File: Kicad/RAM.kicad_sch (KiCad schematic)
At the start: 14 parts, among them U6 74LVC245, U7 74LVC245, U8 MT48LC4M16A2P

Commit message: PCB: Start routing PCB
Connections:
- net D0: now also U7.18 (B0); no longer U6.18 (B0)
- net D1: now also U7.17 (B1); no longer U6.17 (B1)
- net D10: now also U6.16 (B2); no longer U7.16 (B2)
- net D11: now also U6.15 (B3); no longer U7.15 (B3)
- net D12: now also U6.14 (B4); no longer U7.14 (B4)
- net D13: now also U6.13 (B5); no longer U7.13 (B5)
- net D14: now also U6.12 (B6); no longer U7.12 (B6)
- net D15: now also U6.11 (B7); no longer U7.11 (B7)
- net D2: now also U7.16 (B2); no longer U6.16 (B2)
- net D3: now also U7.15 (B3); no longer U6.15 (B3)
- net D4: now also U7.14 (B4); no longer U6.14 (B4)
- net D5: now also U7.11 (B7); no longer U6.11 (B7)
- net D6: now also U7.12 (B6); no longer U6.12 (B6)
- net D7: now also U7.13 (B5); no longer U6.13 (B5)
- net D8: now also U6.18 (B0); no longer U7.18 (B0)
- net D9: now also U6.17 (B1); no longer U7.17 (B1)
- net R_D0: now also U7.2 (A0), U8.2 (DQ0); no longer U6.2 (A0), U8.13 (DQ7)
- net R_D1: now also U7.3 (A1), U8.4 (DQ1); no longer U6.3 (A1), U8.11 (DQ6)
- net R_D10: now also U6.4 (A2), U8.45 (DQ10); no longer U7.4 (A2), U8.50 (DQ13)
- net R_D11: now also U6.5 (A3), U8.47 (DQ11); no longer U7.5 (A3), U8.48 (DQ12)
- net R_D12: now also U6.6 (A4), U8.48 (DQ12); no longer U7.6 (A4), U8.47 (DQ11)
- net R_D13: now also U6.7 (A5), U8.50 (DQ13); no longer U7.7 (A5), U8.45 (DQ10)
- net R_D14: now also U6.8 (A6), U8.51 (DQ14); no longer U7.8 (A6), U8.44 (DQ9)
- net R_D15: now also U6.9 (A7), U8.53 (DQ15); no longer U7.9 (A7), U8.42 (DQ8)
- net R_D2: now also U7.4 (A2), U8.5 (DQ2); no longer U6.4 (A2), U8.10 (DQ5)
- net R_D3: now also U7.5 (A3), U8.7 (DQ3); no longer U6.5 (A3), U8.8 (DQ4)
- net R_D4: now also U7.6 (A4), U8.8 (DQ4); no longer U6.6 (A4), U8.7 (DQ3)
- net R_D5: now also U7.7 (A5), U8.10 (DQ5); no longer U6.7 (A5), U8.5 (DQ2)
- net R_D6: now also U7.8 (A6), U8.11 (DQ6); no longer U6.8 (A6), U8.4 (DQ1)
- net R_D7: now also U7.9 (A7), U8.13 (DQ7); no longer U6.9 (A7), U8.2 (DQ0)
- net R_D8: now also U6.2 (A0), U8.42 (DQ8); no longer U7.2 (A0), U8.53 (DQ15)
- net R_D9: now also U6.3 (A1), U8.44 (DQ9); no longer U7.3 (A1), U8.51 (DQ14)
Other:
- moved on the sheet: C15, C16, C17, C18, C19, C20, C21, C22, C23, C24, C25, U6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

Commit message: PCB: More routing...
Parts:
- U8: value MT48LC4M16A2P -> MT48LC8M16A2P
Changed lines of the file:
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@@
     (in_bom yes) (on_board yes) (fields_autoplaced)
     (property "Reference" "U8" (id 0) (at 182.245 98.425 0))
-    (property "Value" "MT48LC4M16A2P" (id 1) (at 182.245 100.965 0))
+    (property "Value" "MT48LC8M16A2P" (id 1) (at 182.245 100.965 0))
     (property "Footprint" "Package_SO:TSOP-II-54_22.2x10.16mm_P0.8mm" (id 2) (at 153.67 92.71 0)
       (effects (font (size 1.27 1.27)) hide)
     )
-    (property "Datasheet" "" (id 3) (at 153.67 92.71 0)
+    (property "Datasheet" "https://media.digikey.com/pdf/Data%20Sheets/Micron%20Technology%20Inc%20PDFs/MT48LC%208M16A2,16M8A2,32M4A2.pdf" (id 3) (at 153.67 92.71 0)
       (effects (font (size 1.27 1.27)) hide)
     )
@@
     (in_bom yes) (on_board yes) (fields_autoplaced)
     (property "Reference" "U8" (id 0) (at 182.88 29.21 0))
-    (property "Value" "MT48LC4M16A2P" (id 1) (at 182.88 31.75 0))
+    (property "Value" "MT48LC8M16A2P" (id 1) (at 182.88 31.75 0))
     (property "Footprint" "Package_SO:TSOP-II-54_22.2x10.16mm_P0.8mm" (id 2) (at 154.305 43.815 0)
       (effects (font (size 1.27 1.27)) hide)
     )
-    (property "Datasheet" "" (id 3) (at 154.305 43.815 0)
+    (property "Datasheet" "https://media.digikey.com/pdf/Data%20Sheets/Micron%20Technology%20Inc%20PDFs/MT48LC%208M16A2,16M8A2,32M4A2.pdf" (id 3) (at 154.305 43.815 0)
       (effects (font (size 1.27 1.27)) hide)
     )

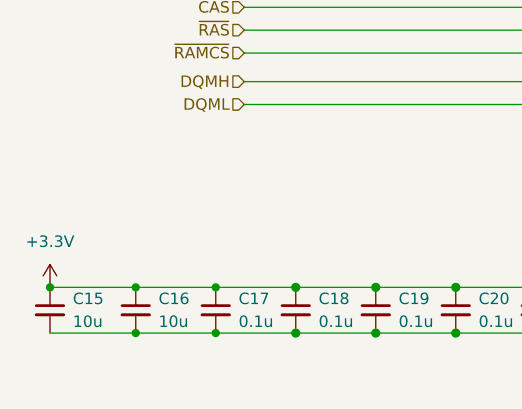
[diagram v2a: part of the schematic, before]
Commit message: PCB: More work...
* Add DIP Switches for Ram/Rom/IDE config
* Route bank select signals for Flash rom
* Flip IDE to bottom of the board
* Add some bulk capacitors
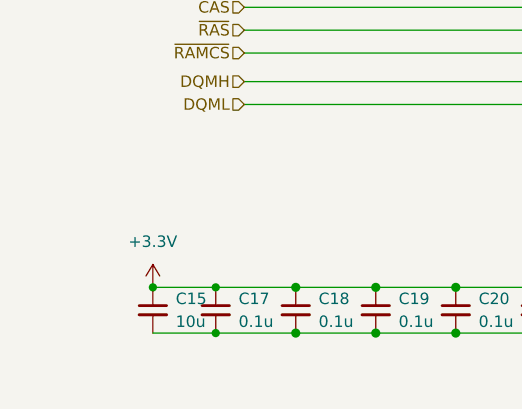
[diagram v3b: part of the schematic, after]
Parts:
- removed C16: 10u, Capacitor_SMD:C_0805_2012Metric_Pad1.18x1.45mm_HandSolder, symbol Device:C_Small
- C15: footprint Capacitor_SMD:C_0805_2012Metric_Pad1.18x1.45mm_HandSolder -> Capacitor_Tantalum_SMD:CP_EIA-3216-18_Kemet-A; LCSC # C15850 -> C117023
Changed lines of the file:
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@@
   (junction (at 170.815 116.205) (diameter 1.016) (color 0 0 0 0)
   )
-  (junction (at 85.09 189.23) (diameter 0) (color 0 0 0 0)
-  )
-  (junction (at 75.565 184.15) (diameter 0) (color 0 0 0 0)
+  (junction (at 86.995 184.15) (diameter 0) (color 0 0 0 0)
   )
   (junction (at 193.675 108.585) (diameter 1.016) (color 0 0 0 0)
@@
   (junction (at 120.65 184.15) (diameter 1.016) (color 0 0 0 0)
   )
-  (junction (at 85.09 184.15) (diameter 0) (color 0 0 0 0)
-  )
   (junction (at 170.815 106.045) (diameter 1.016) (color 0 0 0 0)
   )
@@
     (stroke (width 0) (type default) (color 0 0 0 0))
   )
-  (wire (pts (xy 85.09 189.23) (xy 93.98 189.23))
-    (stroke (width 0) (type default) (color 0 0 0 0))
-  )
   (wire (pts (xy 165.1 44.45) (xy 170.18 44.45))
     (stroke (width 0) (type default) (color 0 0 0 0))
@@
     (stroke (width 0) (type default) (color 0 0 0 0))
   )
+  (wire (pts (xy 86.995 184.15) (xy 93.98 184.15))
+    (stroke (width 0) (type default) (color 0 0 0 0))
+  )
+  (wire (pts (xy 86.995 189.23) (xy 93.98 189.23))
+    (stroke (width 0) (type default) (color 0 0 0 0))
+  )
   (bus (pts (xy 105.41 95.25) (xy 105.41 97.79))
     (stroke (width 0) (type default) (color 0 0 0 0))
@@
     (stroke (width 0) (type default) (color 0 0 0 0))
   )
-  (wire (pts (xy 75.565 189.23) (xy 85.09 189.23))
-    (stroke (width 0) (type default) (color 0 0 0 0))
-  )
   (bus (pts (xy 105.41 34.29) (xy 105.41 36.83))
     (stroke (width 0) (type default) (color 0 0 0 0))
@@
     (stroke (width 0) (type solid) (color 0 0 0 0))
   )
-  (wire (pts (xy 85.09 184.15) (xy 93.98 184.15))
-    (stroke (width 0) (type default) (color 0 0 0 0))
-  )
   (wire (pts (xy 165.1 54.61) (xy 170.18 54.61))
     (stroke (width 0) (type default) (color 0 0 0 0))
@@
   )
   (wire (pts (xy 195.58 49.53) (xy 201.93 49.53))
-    (stroke (width 0) (type default) (color 0 0 0 0))
-  )
-  (wire (pts (xy 75.565 184.15) (xy 85.09 184.15))
     (stroke (width 0) (type default) (color 0 0 0 0))
   )
@@
     )
     (property "LCSC #" "C14663" (id 4) (at 156.21 186.69 0)
+      (effects (font (size 1.27 1.27)) hide)
+    )
+    (pin "1")
+    (pin "2")
+  )
+  (symbol (lib_id "Device:C_Small") (at 86.995 186.69 0) (unit 1)
+    (in_bom yes) (on_board yes) (fields_autoplaced)
+    (property "Reference" "C15" (id 0) (at 89.535 185.4199 0)
+      (effects (font (size 1.27 1.27)) (justify left))
+    )
+    (property "Value" "10u" (id 1) (at 89.535 187.9599 0)
+      (effects (font (size 1.27 1.27)) (justify left))
+    )
+    (property "Footprint" "Capacitor_Tantalum_SMD:CP_EIA-3216-18_Kemet-A" (id 2) (at 86.995 186.69 0)
+      (effects (font (size 1.27 1.27)) hide)
+    )
+    (property "Datasheet" "~" (id 3) (at 86.995 186.69 0)
+      (effects (font (size 1.27 1.27)) hide)
+    )
+    (property "LCSC #" "C117023" (id 4) (at 86.995 186.69 0)
       (effects (font (size 1.27 1.27)) hide)
     )
@@
     )
     (property "LCSC #" "C14663" (id 4) (at 129.54 186.69 0)
-      (effects (font (size 1.27 1.27)) hide)
-    )
-    (pin "1")
-    (pin "2")
-  )
-  (symbol (lib_id "Device:C_Small") (at 85.09 186.69 0) (unit 1)
-    (in_bom yes) (on_board yes) (fields_autoplaced)
-    (property "Reference" "C16" (id 0) (at 87.63 185.4199 0)
-      (effects (font (size 1.27 1.27)) (justify left))
-    )
-    (property "Value" "10u" (id 1) (at 87.63 187.9599 0)
-      (effects (font (size 1.27 1.27)) (justify left))
-    )
-    (property "Footprint" "Capacitor_SMD:C_0805_2012Metric_Pad1.18x1.45mm_HandSolder" (id 2) (at 85.09 186.69 0)
-      (effects (font (size 1.27 1.27)) hide)
-    )
-    (property "Datasheet" "~" (id 3) (at 85.09 186.69 0)
-      (effects (font (size 1.27 1.27)) hide)
-    )
-    (property "LCSC #" "C15850" (id 4) (at 85.09 186.69 0)
-      (effects (font (size 1.27 1.27)) hide)
-    )
-    (pin "1")
-    (pin "2")
-  )
-  (symbol (lib_id "Device:C_Small") (at 75.565 186.69 0) (unit 1)
-    (in_bom yes) (on_board yes) (fields_autoplaced)
-    (property "Reference" "C15" (id 0) (at 78.105 185.4199 0)
-      (effects (font (size 1.27 1.27)) (justify left))
-    )
-    (property "Value" "10u" (id 1) (at 78.105 187.9599 0)
-      (effects (font (size 1.27 1.27)) (justify left))
-    )
-    (property "Footprint" "Capacitor_SMD:C_0805_2012Metric_Pad1.18x1.45mm_HandSolder" (id 2) (at 75.565 186.69 0)
-      (effects (font (size 1.27 1.27)) hide)
-    )
-    (property "Datasheet" "~" (id 3) (at 75.565 186.69 0)
-      (effects (font (size 1.27 1.27)) hide)
-    )
-    (property "LCSC #" "C15850" (id 4) (at 75.565 186.69 0)
       (effects (font (size 1.27 1.27)) hide)
     )
@@
     (pin "1")
   )
-  (symbol (lib_id "power:+3.3V") (at 75.565 184.15 0) (unit 1)
-    (in_bom yes) (on_board yes) (fields_autoplaced)
-    (property "Reference" "#PWR041" (id 0) (at 75.565 187.96 0)
-      (effects (font (size 1.27 1.27)) hide)
-    )
-    (property "Value" "+3.3V" (id 1) (at 75.565 179.07 0))
-    (property "Footprint" "" (id 2) (at 75.565 184.15 0)
-      (effects (font (size 1.27 1.27)) hide)
-    )
-    (property "Datasheet" "" (id 3) (at 75.565 184.15 0)
-      (effects (font (size 1.27 1.27)) hide)
-    )
+  (symbol (lib_id "power:+3.3V") (at 86.995 184.15 0) (unit 1)
+    (in_bom yes) (on_board yes) (fields_autoplaced)
+    (property "Reference" "#PWR041" (id 0) (at 86.995 187.96 0)
+      (effects (font (size 1.27 1.27)) hide)
+    )
+    (property "Value" "+3.3V" (id 1) (at 86.995 179.07 0))
+    (property "Footprint" "" (id 2) (at 86.995 184.15 0)
+      (effects (font (size 1.27 1.27)) hide)
+    )
+    (property "Datasheet" "" (id 3) (at 86.995 184.15 0)
+      (effects (font (size 1.27 1.27)) hide)
+    )

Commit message: PCB: Route Flash bank switch jumper
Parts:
- C15: LCSC # C117023 -> C7171
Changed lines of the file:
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@@
       (effects (font (size 1.27 1.27)) hide)
     )
-    (property "LCSC #" "C117023" (id 4) (at 86.995 186.69 0)
+    (property "LCSC #" "C7171" (id 4) (at 86.995 186.69 0)
       (effects (font (size 1.27 1.27)) hide)
     )

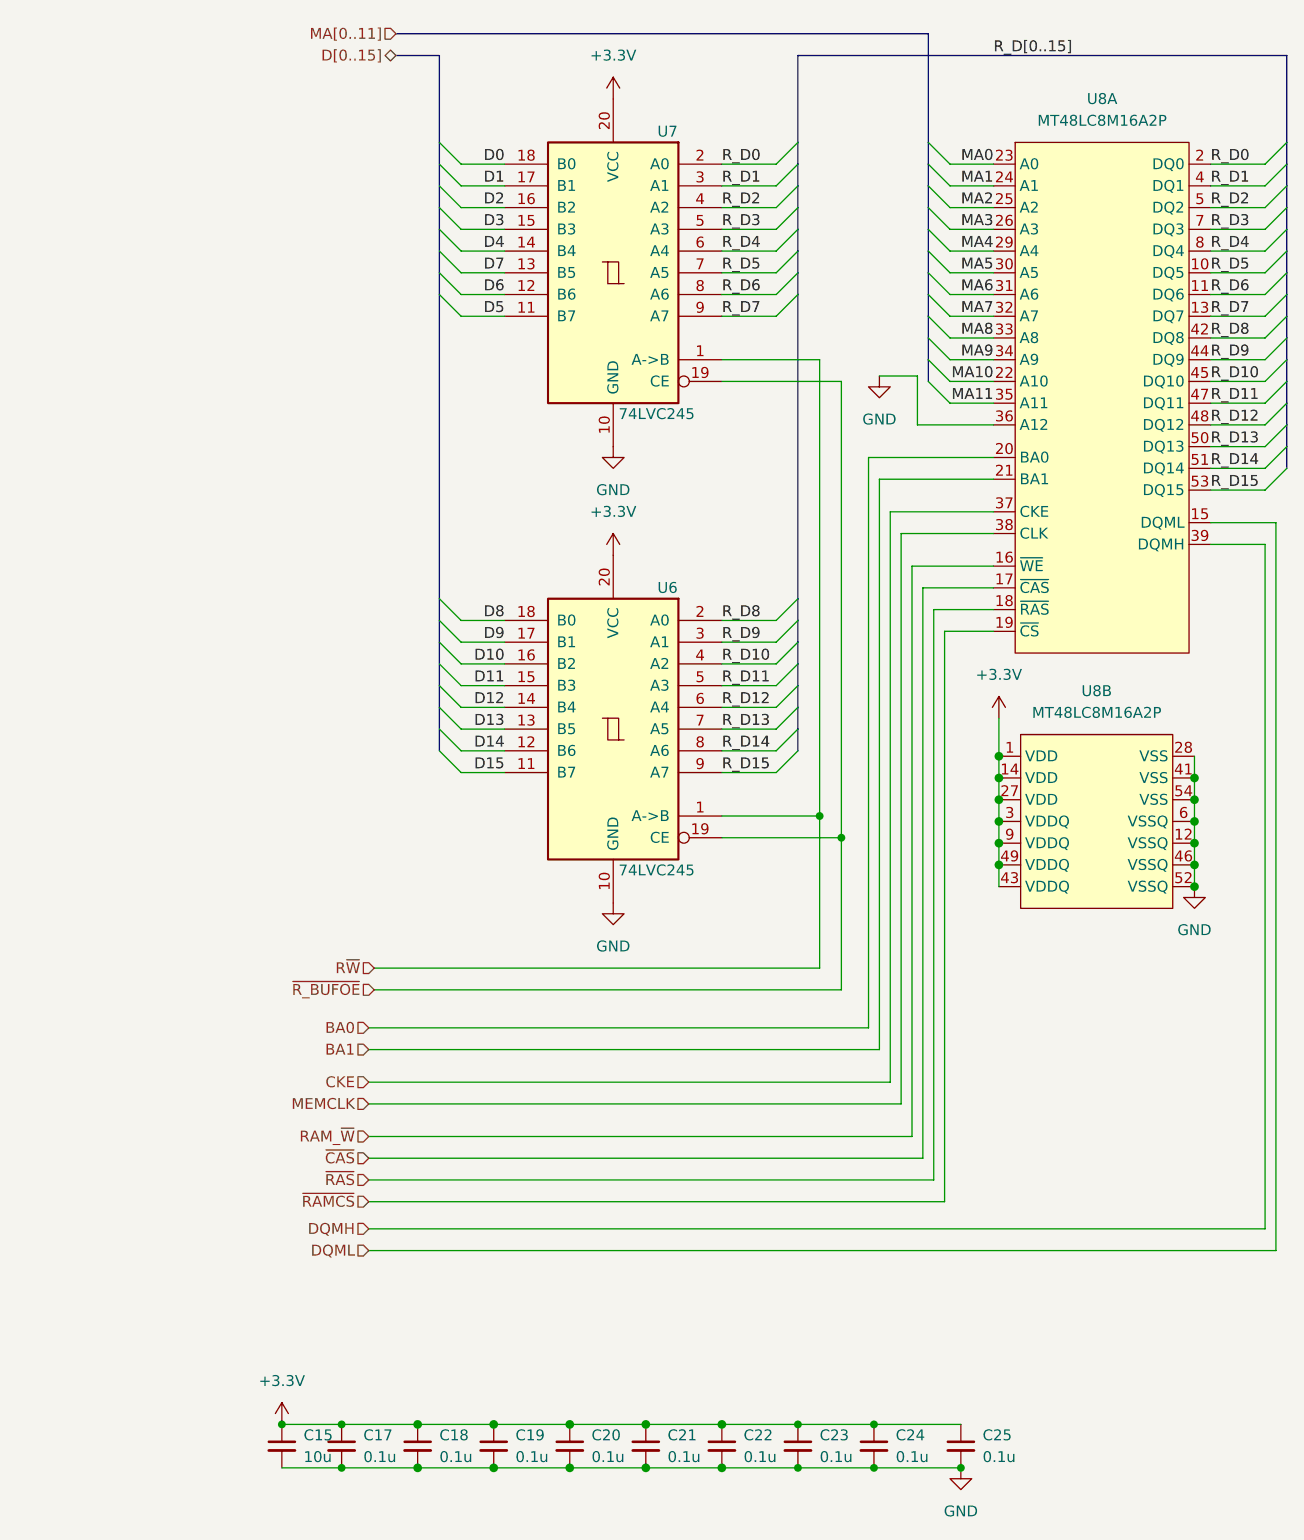
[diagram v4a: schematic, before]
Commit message: PCB: Add 22 Ohm series resistors for SDRAM
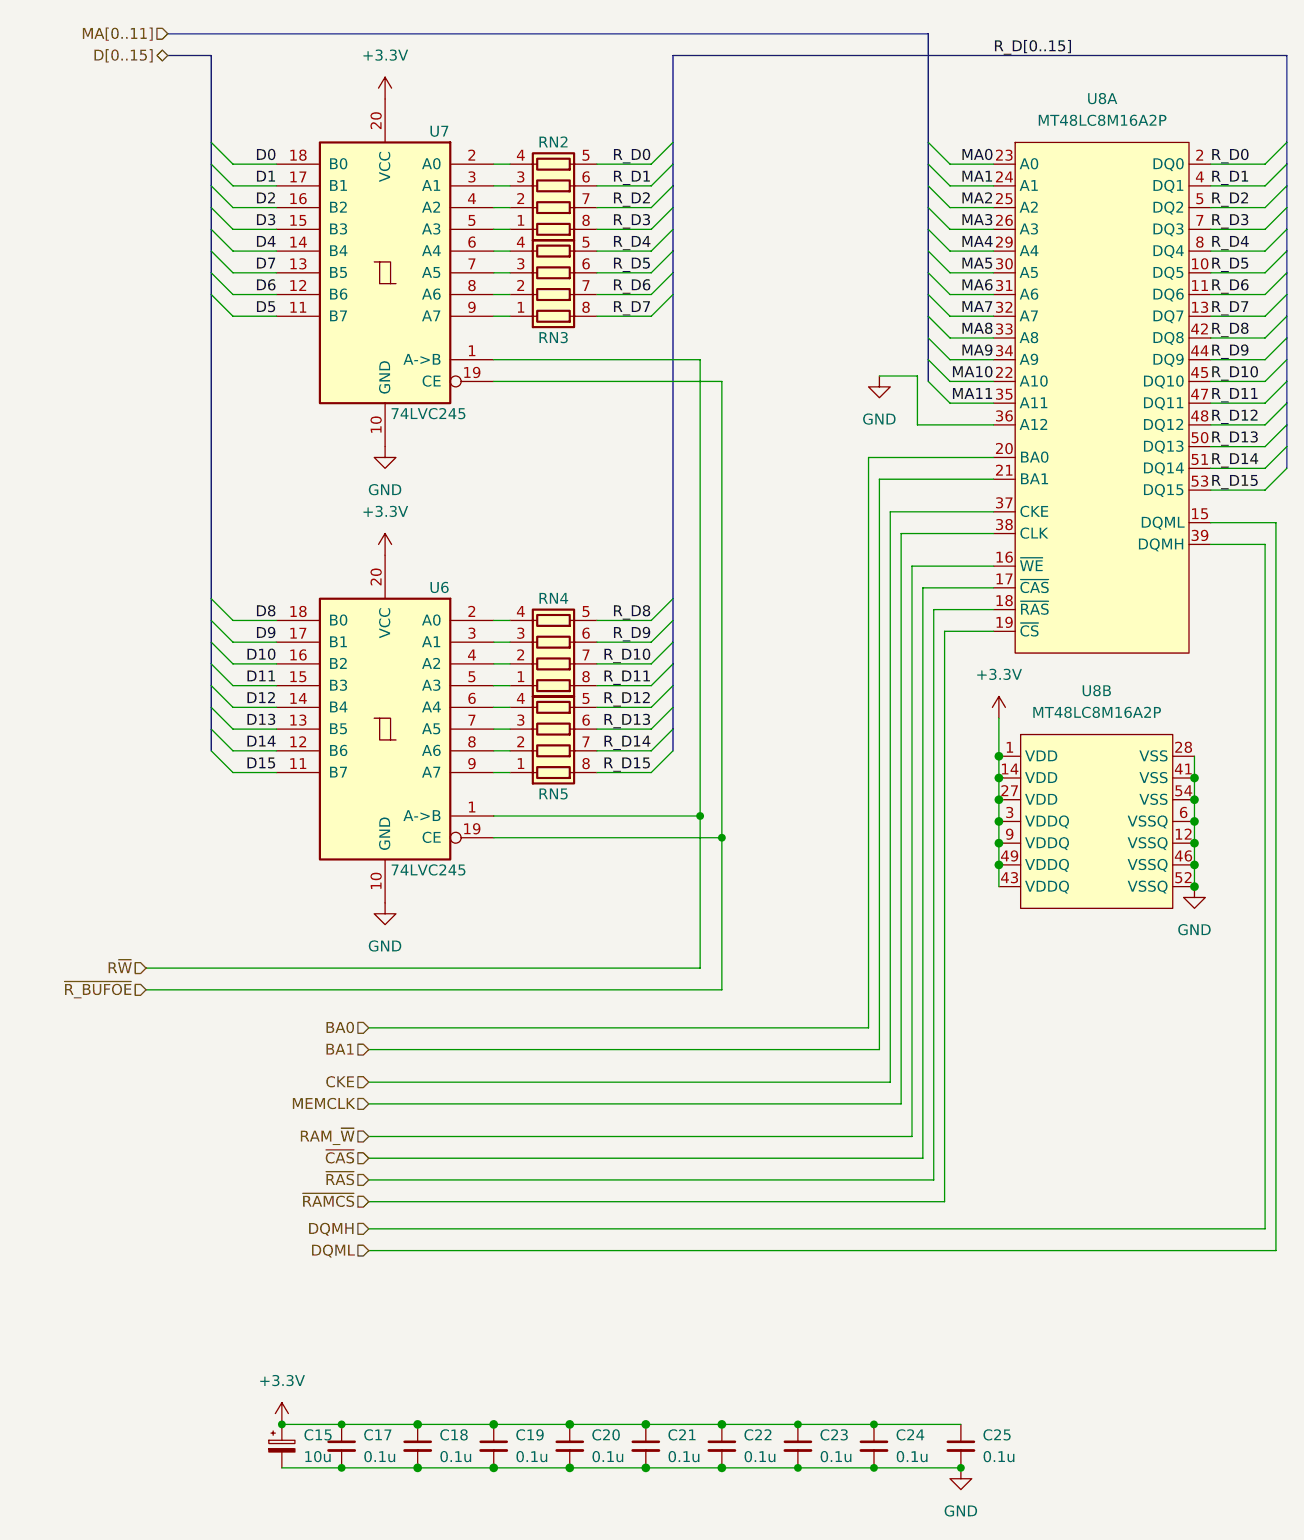
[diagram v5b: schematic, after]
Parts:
- added RN2, RN3, RN4, RN5: R_Pack04, Resistor_SMD:R_Array_Convex_4x0603, symbol Device:R_Pack04
- C15: symbol Device:C_Small -> Device:C_Polarized_Small
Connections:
- net R_D0: now also RN2.5 (R4.2); no longer U7.2 (A0)
- net R_D1: now also RN2.6 (R3.2); no longer U7.3 (A1)
- net R_D10: now also RN4.7 (R2.2); no longer U6.4 (A2)
- net R_D11: now also RN4.8 (R1.2); no longer U6.5 (A3)
- net R_D12: now also RN5.5 (R4.2); no longer U6.6 (A4)
- net R_D13: now also RN5.6 (R3.2); no longer U6.7 (A5)
- net R_D14: now also RN5.7 (R2.2); no longer U6.8 (A6)
- net R_D15: now also RN5.8 (R1.2); no longer U6.9 (A7)
- net R_D2: now also RN2.7 (R2.2); no longer U7.4 (A2)
- net R_D3: now also RN2.8 (R1.2); no longer U7.5 (A3)
- net R_D4: now also RN3.5 (R4.2); no longer U7.6 (A4)
- net R_D5: now also RN3.6 (R3.2); no longer U7.7 (A5)
- net R_D6: now also RN3.7 (R2.2); no longer U7.8 (A6)
- net R_D7: now also RN3.8 (R1.2); no longer U7.9 (A7)
- net R_D8: now also RN4.5 (R4.2); no longer U6.2 (A0)
- net R_D9: now also RN4.6 (R3.2); no longer U6.3 (A1)
- new net: RN4.1 (R1.1), U6.5 (A3)
- new net: RN4.2 (R2.1), U6.4 (A2)
- new net: RN4.3 (R3.1), U6.3 (A1)
- new net: RN4.4 (R4.1), U6.2 (A0)
- new net: RN5.4 (R4.1), U6.6 (A4)
- new net: RN5.3 (R3.1), U6.7 (A5)
- new net: RN5.2 (R2.1), U6.8 (A6)
- new net: RN5.1 (R1.1), U6.9 (A7)
- new net: RN3.1 (R1.1), U7.9 (A7)
- new net: RN3.2 (R2.1), U7.8 (A6)
- new net: RN3.3 (R3.1), U7.7 (A5)
- new net: RN3.4 (R4.1), U7.6 (A4)
- new net: RN2.4 (R4.1), U7.2 (A0)
- new net: RN2.3 (R3.1), U7.3 (A1)
- new net: RN2.2 (R2.1), U7.4 (A2)
- new net: RN2.1 (R1.1), U7.5 (A3)
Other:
- moved on the sheet: U6, U7
